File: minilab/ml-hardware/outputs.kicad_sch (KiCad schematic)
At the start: 24 parts, among them SW1 SW_Push, SW2 SW_Push, SW3 SW_Push, SW4 SW_Push, SW5 SW_Push, SW6 SW_Push, SW7 SW_Push, SW8 SW_Push

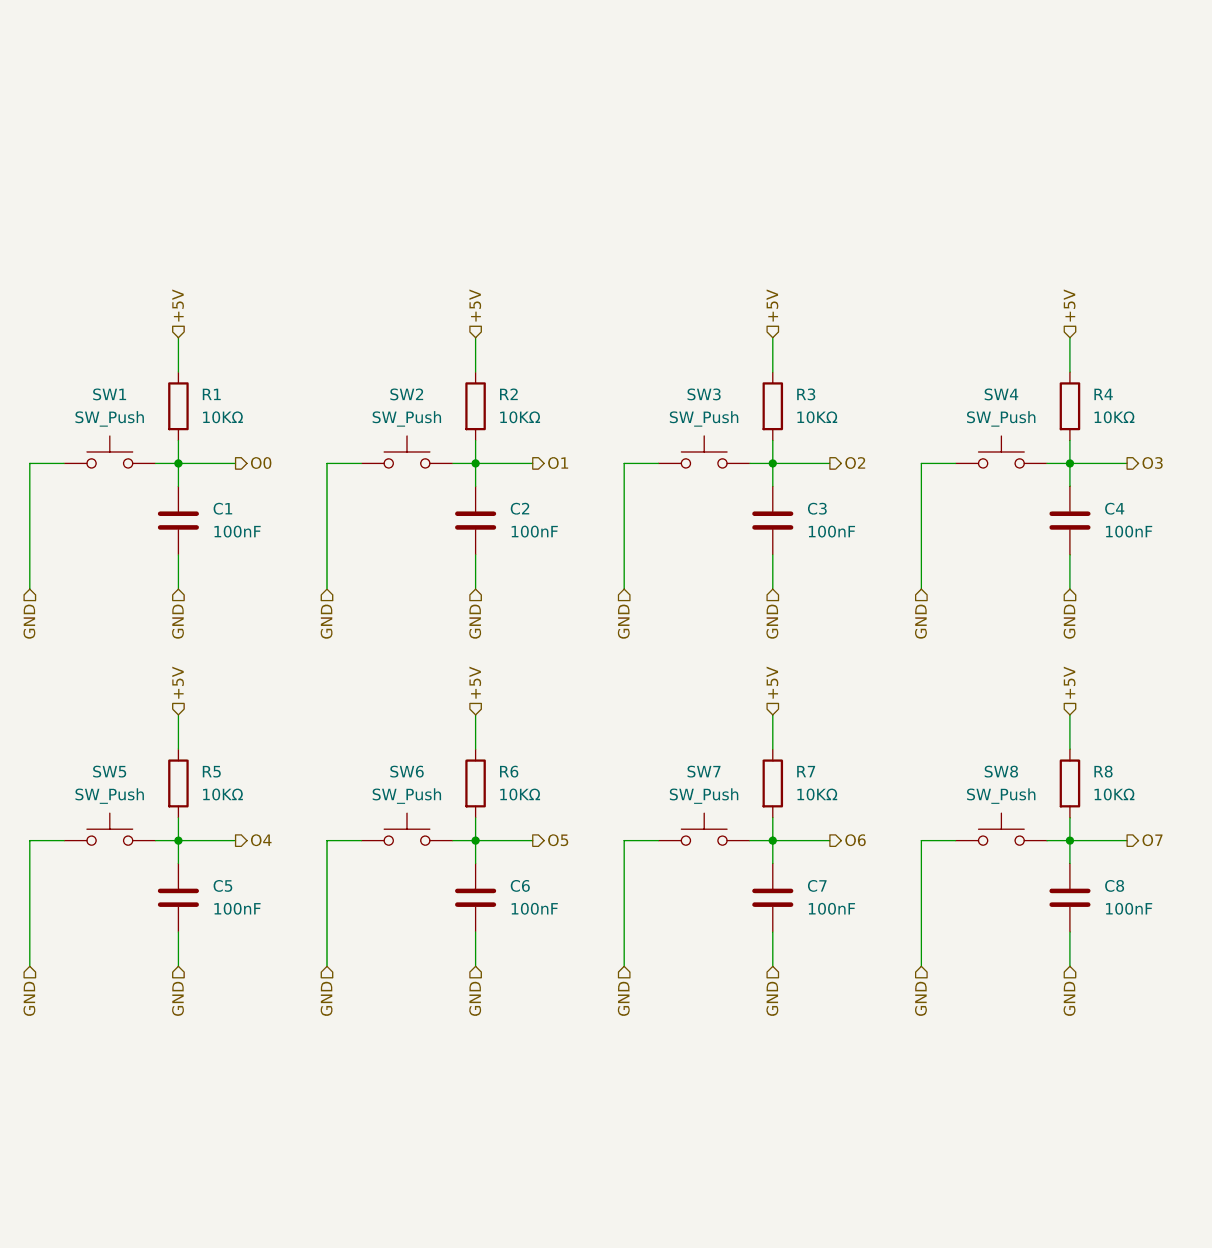
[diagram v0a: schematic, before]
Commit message: minilab: Enforce "pcb/page" hierarchy on schematic
This does not apply (necessarily) to subpages.
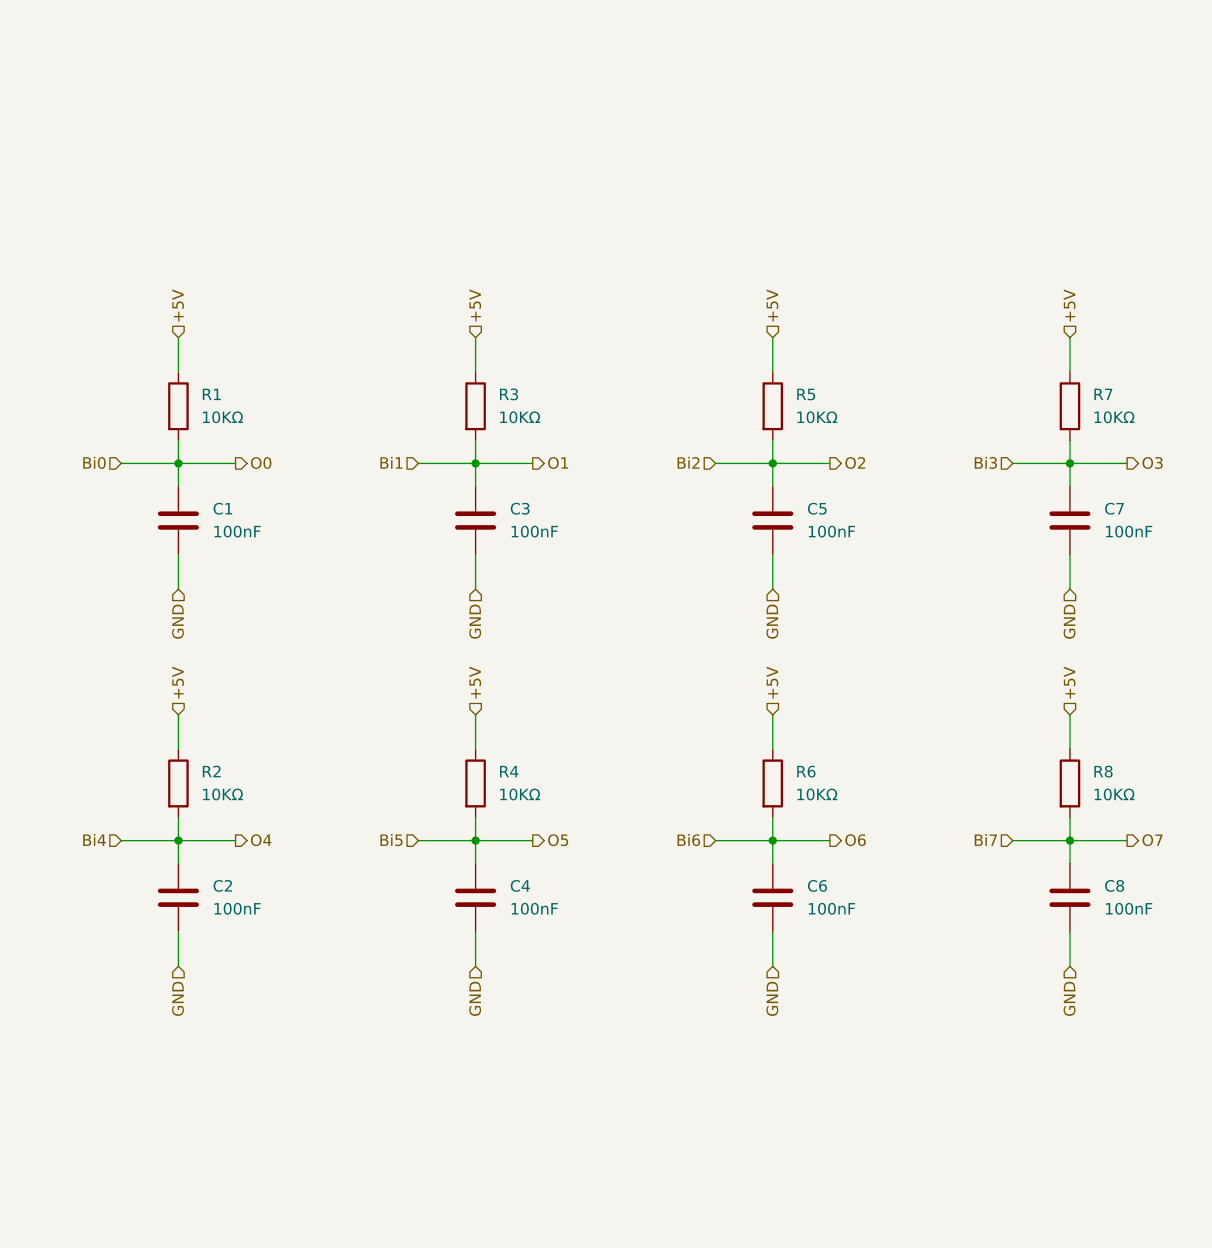
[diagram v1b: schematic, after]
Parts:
- removed SW1, SW2, SW3, SW4, SW5, SW6, SW7, SW8: SW_Push, symbol Switch:SW_Push
- C1, C8: footprint (none) -> Capacitor_THT:C_Disc_D6.0mm_W2.5mm_P5.00mm
- C2: renamed from C5; footprint (none) -> Capacitor_THT:C_Disc_D6.0mm_W2.5mm_P5.00mm
- C3: renamed from C2; footprint (none) -> Capacitor_THT:C_Disc_D6.0mm_W2.5mm_P5.00mm
- C4: renamed from C6; footprint (none) -> Capacitor_THT:C_Disc_D6.0mm_W2.5mm_P5.00mm
- C5: renamed from C3; footprint (none) -> Capacitor_THT:C_Disc_D6.0mm_W2.5mm_P5.00mm
- C6: renamed from C7; footprint (none) -> Capacitor_THT:C_Disc_D6.0mm_W2.5mm_P5.00mm
- C7: renamed from C4; footprint (none) -> Capacitor_THT:C_Disc_D6.0mm_W2.5mm_P5.00mm
- R1, R8: footprint (none) -> Resistor_THT:R_Axial_DIN0204_L3.6mm_D1.6mm_P5.08mm_Horizontal
- R2: renamed from R5; footprint (none) -> Resistor_THT:R_Axial_DIN0204_L3.6mm_D1.6mm_P5.08mm_Horizontal
- R3: renamed from R2; footprint (none) -> Resistor_THT:R_Axial_DIN0204_L3.6mm_D1.6mm_P5.08mm_Horizontal
- R4: renamed from R6; footprint (none) -> Resistor_THT:R_Axial_DIN0204_L3.6mm_D1.6mm_P5.08mm_Horizontal
- R5: renamed from R3; footprint (none) -> Resistor_THT:R_Axial_DIN0204_L3.6mm_D1.6mm_P5.08mm_Horizontal
- R6: renamed from R7; footprint (none) -> Resistor_THT:R_Axial_DIN0204_L3.6mm_D1.6mm_P5.08mm_Horizontal
- R7: renamed from R4; footprint (none) -> Resistor_THT:R_Axial_DIN0204_L3.6mm_D1.6mm_P5.08mm_Horizontal
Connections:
- net O0 renamed Bi0
- net O1 renamed Bi1
- net O2 renamed Bi2
- net O3 renamed Bi3
- net O4 renamed Bi4
- net O5 renamed Bi5
- net O6 renamed Bi6
- net O7 renamed Bi7

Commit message: minilab: Agrega 2da opc conectores y modelos 3d
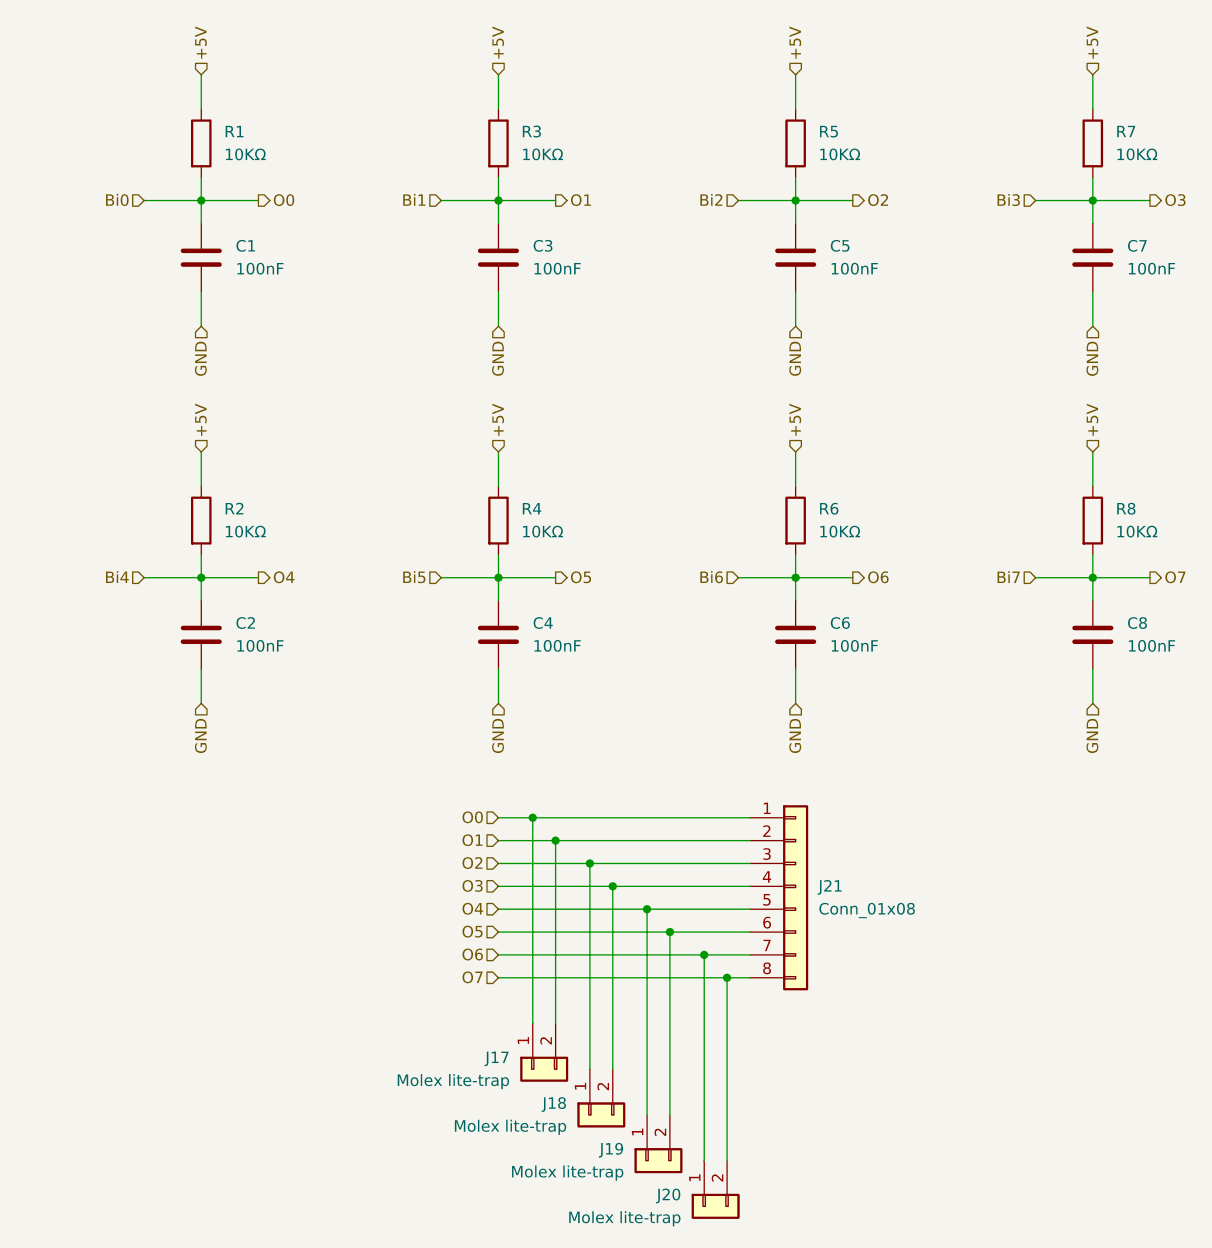
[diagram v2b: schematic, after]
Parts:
- added J17, J18, J19, J20: Molex lite-trap, Extras:104238-0210, symbol Connector_Generic:Conn_01x02
- added J21: Conn_01x08, Connector_PinSocket_2.54mm:PinSocket_1x08_P2.54mm_Horizontal, symbol Connector_Generic:Conn_01x08
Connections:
- net Bi0: now also J17.1 (Pin_1), J21.1 (Pin_1)
- net Bi1: now also J17.2 (Pin_2), J21.2 (Pin_2)
- net Bi2: now also J18.1 (Pin_1), J21.3 (Pin_3)
- net Bi3: now also J18.2 (Pin_2), J21.4 (Pin_4)
- net Bi4: now also J19.1 (Pin_1), J21.5 (Pin_5)
- net Bi5: now also J19.2 (Pin_2), J21.6 (Pin_6)
- net Bi6: now also J20.1 (Pin_1), J21.7 (Pin_7)
- net Bi7: now also J20.2 (Pin_2), J21.8 (Pin_8)
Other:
- moved on the sheet: C1, C2, C3, C4, C5, C6, C7, C8, R1, R2, R3, R4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

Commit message: minilab: Corrige huella molex microfit y edge-*-02
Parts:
- J17, J18, J19, J20: footprint Extras:104238-0210 -> Extras:Molex-Lite_trap
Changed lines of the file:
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@@
 			)
 		)
-		(property "Footprint" "Extras:104238-0210"
+		(property "Footprint" "Extras:Molex-Lite_trap"
 			(at 156.21 161.29 0)
 			(effects
@@
 			)
 		)
-		(property "Footprint" "Extras:104238-0210"
+		(property "Footprint" "Extras:Molex-Lite_trap"
 			(at 143.51 151.13 0)
 			(effects
@@
 			)
 		)
-		(property "Footprint" "Extras:104238-0210"
+		(property "Footprint" "Extras:Molex-Lite_trap"
 			(at 137.16 146.05 0)
 			(effects
@@
 			)
 		)
-		(property "Footprint" "Extras:104238-0210"
+		(property "Footprint" "Extras:Molex-Lite_trap"
 			(at 149.86 156.21 0)
 			(effects
